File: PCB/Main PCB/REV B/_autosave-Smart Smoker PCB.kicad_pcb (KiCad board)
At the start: 4 copper layers, 120 x 60 mm, 90 parts, among them J1 1051330001, J10 Ignitor, J11 Auger, J12 FAN, J2 393570002, J3 393570002, J4 393570002, J5 393570002, J6 393570002, J7 Hopper, J8 Lid, J9 MEM2051-00-195-00-A, K1 CPC1966Y, Q1 25V 1.5A Trans, Q2 25V 1.5A Trans, SW1 SW_Coded_SH-7050, U1 ESP32-WROOM-32UE_16MB, U2 DG409LEDY-T1-GE3, U3 MAX31855KASA, U4 CP2102N-Axx-xQFN20, U5 AMS1117-3.3, U6 LM66100DCKR, U7 LM66100DCKR, U8 AQH3223A, U9 AQH3223A

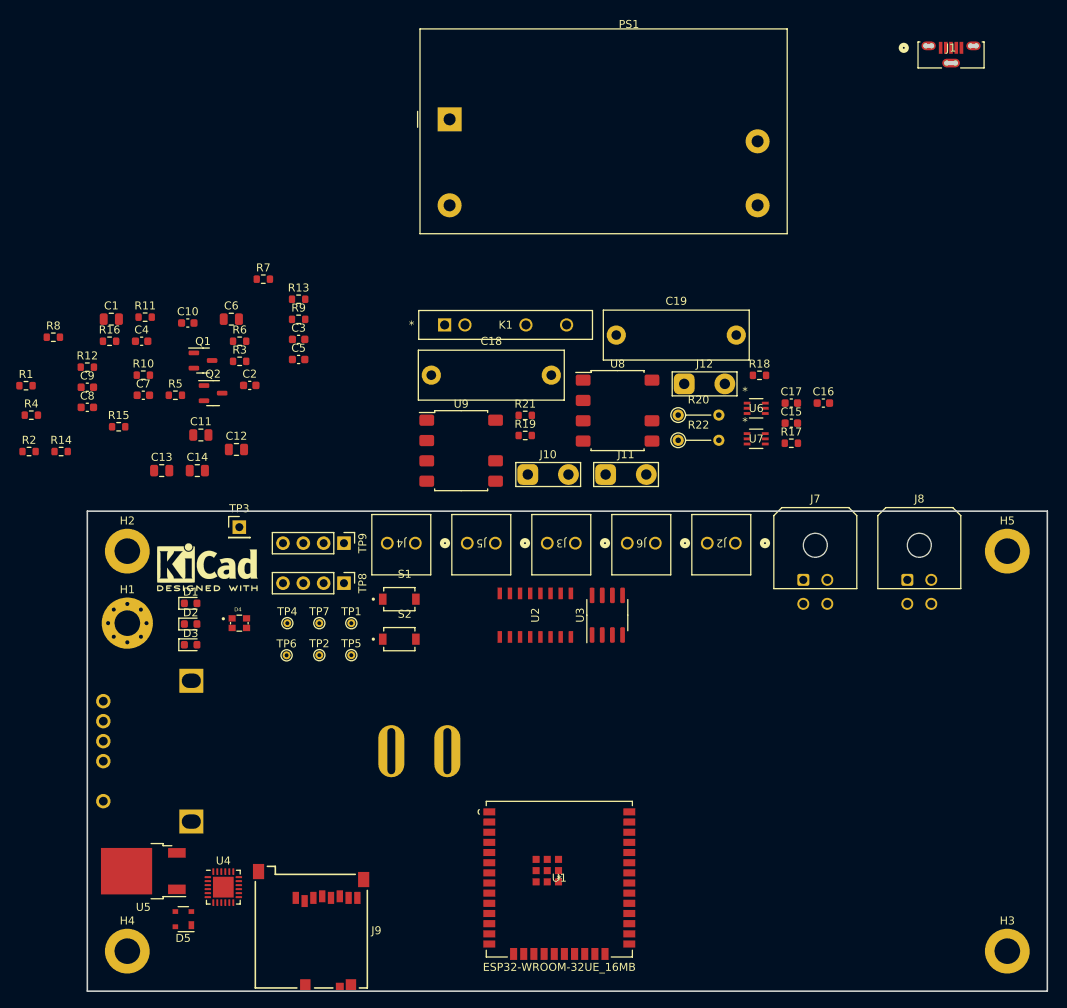
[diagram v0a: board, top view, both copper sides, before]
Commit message: Changed rotary encoder to incremental, nearly done design on rotary encoder
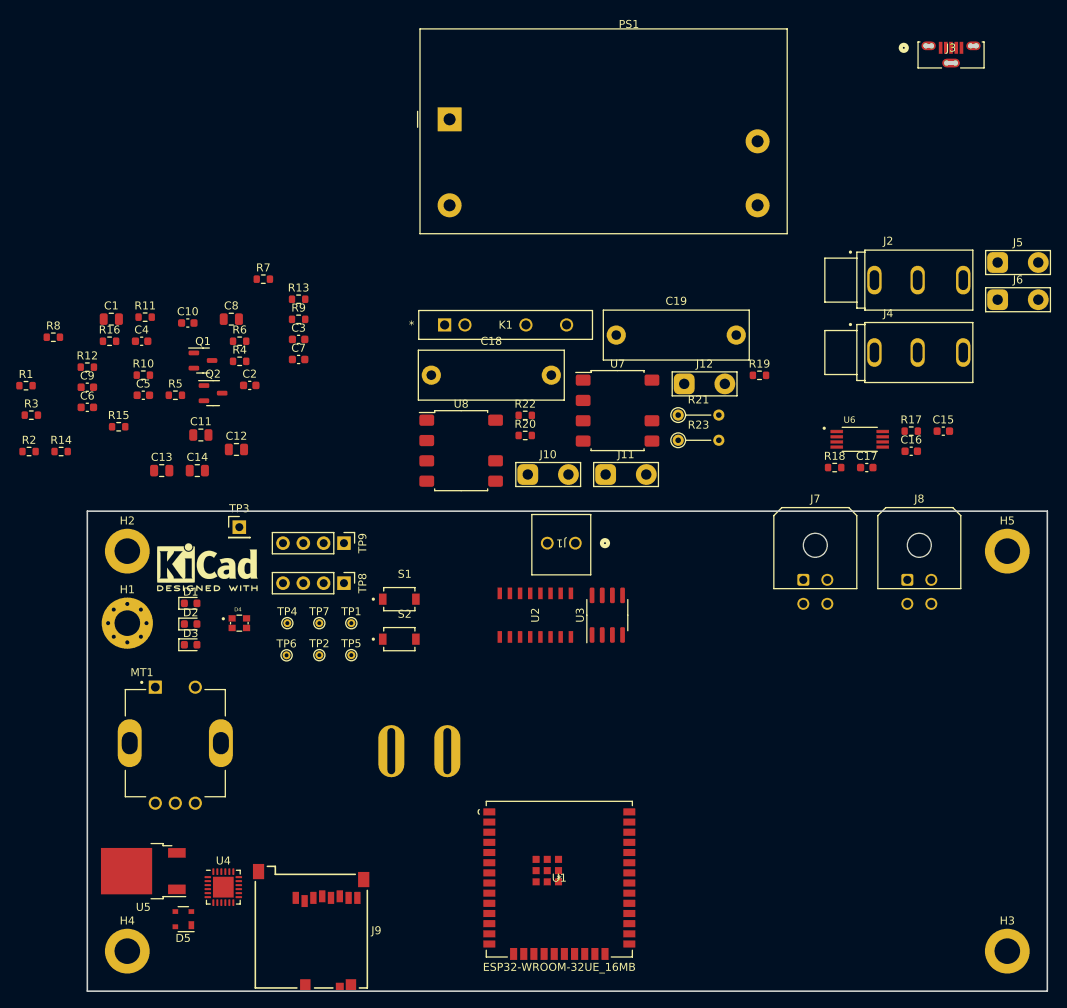
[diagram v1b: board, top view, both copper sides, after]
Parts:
- removed SW1: SW_Coded_SH-7050, Rotary_Encoder:PAC18R1-43D19F
- removed the U7 at (183.6, 91.0)
- added MT1: PEC11R-4215F-S0024, Customs Smoker:XDCR_PEC11R-4215F-S0024, F.Cu at (111.0, 129.0)
- added R18: 250Ohm 0.1% 0603, Resistor_SMD:R_0603_1608Metric, F.Cu at (193.4, 94.5)
- C15: value 0.1uF 50V X7R 0603 -> 1uF 16V X7R 0603
- C16: value 1uF 25V X5R 0603 -> 0.1uF 50V X7R 0603
- J2, J4: value 393570002 -> MJ-3502; footprint Customs Smoker:CONN_393570002_MOL -> Customs Smoker:CUI_MJ-3502
- J5, J6: value 393570002 -> MJ-3502; footprint Customs Smoker:CONN_393570002_MOL -> TestPoint:TestPoint_2Pads_Pitch5.08mm_Drill1.3mm
- R17: value 470Ohm 5% 0603 -> 10K 1% 0603
- U6: value LM66100DCKR -> TPS2115APWR; footprint Customs Smoker:DCK6_TEX -> Customs Smoker:SOP65P640X120-8N
- moved J5 71.9 mm to (213.8, 68.9), turned to 0 degrees
- moved J4 67.3 mm to (203.9, 80.2), turned to 0 degrees
- moved J6 52.5 mm to (213.8, 73.6), turned to 0 degrees
- moved J2 40.1 mm to (203.9, 71.1), turned to 0 degrees
- moved C15 19.0 mm to (207.0, 90.0)
- moved R17 15.1 mm to (203.0, 90.0)
- moved U6 13.5 mm to (196.6, 91.0)
- moved C16 12.5 mm to (203.0, 92.5)
- moved C17 12.4 mm to (197.4, 94.5)
- renumbered C7 to C5, C8 to C6, C5 to C7, C6 to C8, J3 to J1, J1 to J3, R18 to R19, R19 to R20, R20 to R21, R21 to R22, R22 to R23, R4 to R3, R3 to R4, U8 to U7, U9 to U8
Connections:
- C15 pad 1: +3.3VP -> GND
- C15 pad 2: GND -> +3.3V
- C16 pad 2: +3.3V -> +3.3VA
- C17 pad 1: +3.3VA -> GND
- C17 pad 2: GND -> +3.3VP
- J2 pad 1: /Probe4+ -> /Probe1-
- J2 pad 2: /Probe4- -> /Probe1+
- J4 pad 1: /Probe1+ -> /Probe2-
- J4 pad 2: /Probe1- -> /Probe2+
- J5 pad 1: /Probe2+ -> /Probe3-
- J5 pad 2: /Probe2- -> /Probe3+
- J6 pad 1: /Probe3+ -> /Probe4-
- J6 pad 2: /Probe3- -> /Probe4+
- R17 pad 1: Net-(R17-Pad1) -> +3.3V
- R17 pad 2: +3.3VP -> /Power/IO_4
- U6 pad 1: +3.3VP -> /Power/IO_4
- U6 pad 2: GND -> unconnected-(U6-Pad2)
- U6 pad 3: +3.3VA -> GND
- U6 pad 4: unconnected-(U6-Pad4) -> Net-(R18-Pad1)
- U6 pad 5: Net-(R17-Pad1) -> GND
- U6 pad 6: +3.3V -> +3.3VA

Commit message: SD card complete. All gpio full
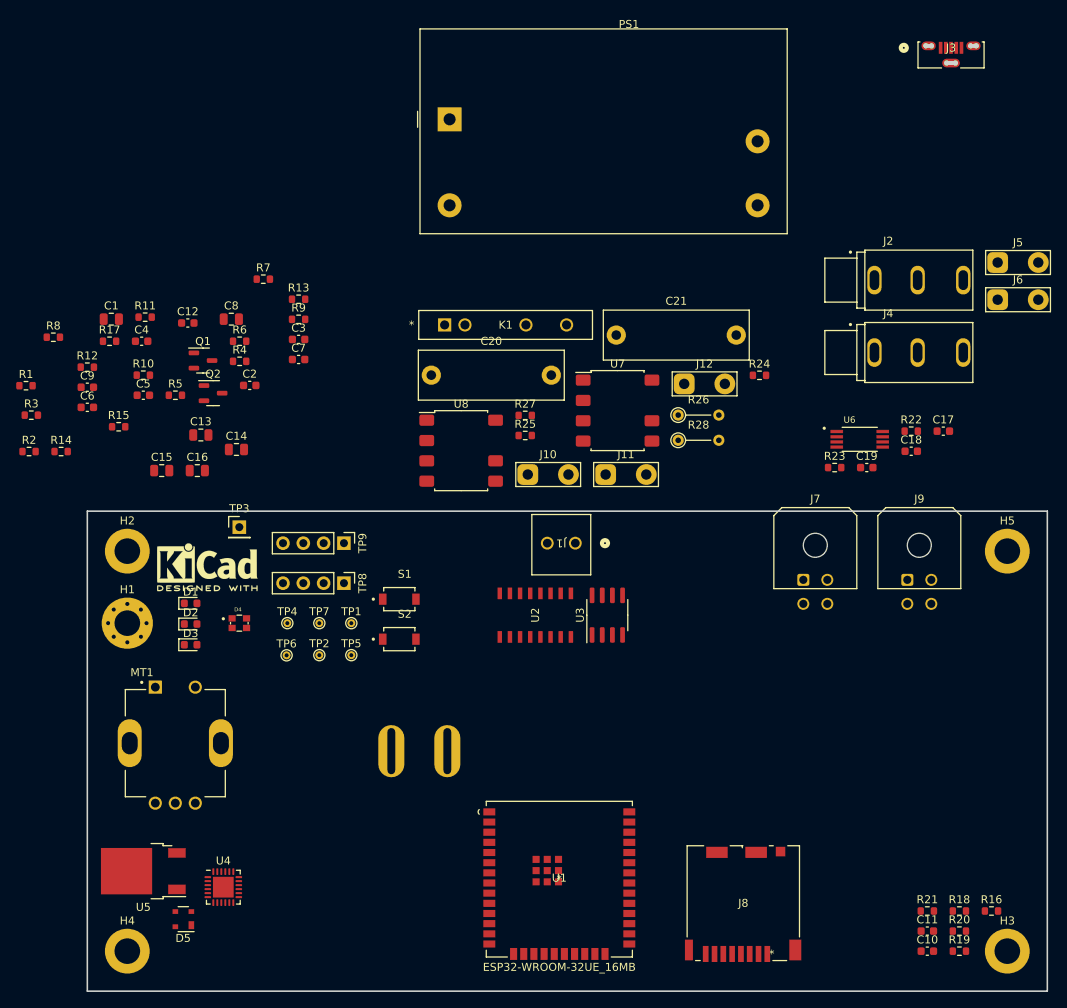
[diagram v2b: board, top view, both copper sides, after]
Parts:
- removed the J9 at (128.0, 152.0)
- added C10: 0.01uF 50V X7R 0603, Capacitor_SMD:C_0603_1608Metric, F.Cu at (205.0, 155.0)
- added C11: 0.01uF 50V X7R 0603, Capacitor_SMD:C_0603_1608Metric, F.Cu at (205.0, 152.5)
- added J8: Micro_SD_Card_Det, Customs Smoker:DM3CS-SF_HIR, F.Cu at (182.0, 149.0)
- added R16: 10K 1% 0603, Resistor_SMD:R_0603_1608Metric, F.Cu at (213.0, 150.0)
- added R18: 10K 1% 0603, Resistor_SMD:R_0603_1608Metric, F.Cu at (209.0, 150.0)
- added R19: 10K 1% 0603, Resistor_SMD:R_0603_1608Metric, F.Cu at (209.0, 155.0)
- added R20: 10K 1% 0603, Resistor_SMD:R_0603_1608Metric, F.Cu at (209.0, 152.5)
- added R21: 10K 1% 0603, Resistor_SMD:R_0603_1608Metric, F.Cu at (205.0, 150.0)
- renumbered C10 to C12, C11 to C13, C12 to C14, C13 to C15, C14 to C16, C15 to C17, C16 to C18, C17 to C19, C18 to C20, C19 to C21, J8 to J9, R16 to R17, R17 to R22, R18 to R23, R19 to R24, R20 to R25, R21 to R26, R22 to R27, R23 to R28
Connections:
- MT1 pad 1: unconnected-(MT1-Pad1) -> GND
- MT1 pad 2: unconnected-(MT1-Pad2) -> /IO34
- MT1 pad A: unconnected-(MT1-PadA) -> Net-(MT1-PadA)
- MT1 pad B: unconnected-(MT1-PadB) -> Net-(MT1-PadB)
- MT1 pad COM: unconnected-(MT1-PadCOM) -> GND
- MT1 pad S1: Net-(MT1-PadS1) -> GND
- MT1 pad S2: Net-(MT1-PadS1) -> GND
- U1 pad 27: /IO16 -> /SPI_MOSI
- U2 pad 16: /IO15 -> /IO16
